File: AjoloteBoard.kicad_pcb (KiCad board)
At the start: 2 copper layers, 69 x 84.9 mm, 9 parts, among them SW1 On

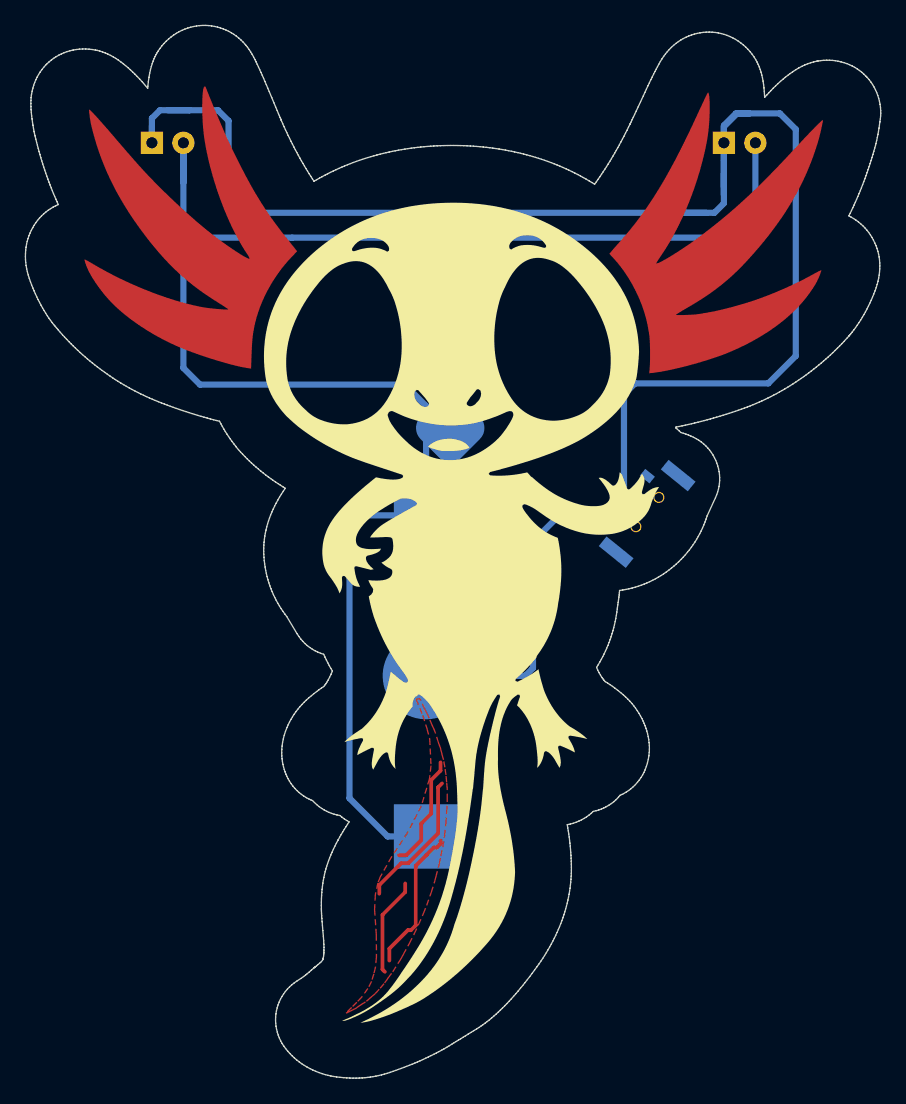
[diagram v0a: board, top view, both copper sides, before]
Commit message: Battery holder and switch changed
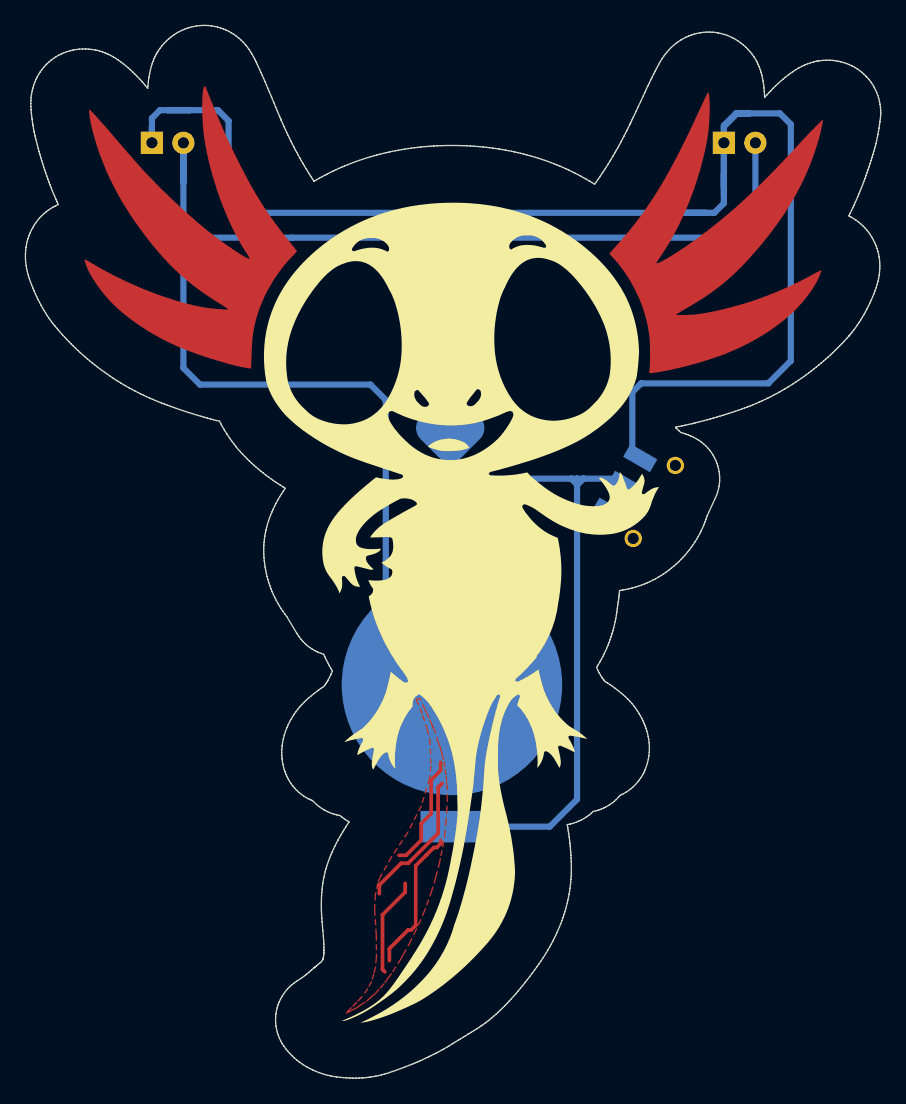
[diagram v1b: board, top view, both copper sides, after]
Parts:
- BT1: footprint footprints:79523141 -> Batteries:BAT-HLD-001
- SW1: footprint footprints:Micro_interruptor_SPDT -> footprints:JS102011SAQN
- moved SW1 4.40 mm to (173.7, 93.1), turned to -120 degrees
- moved BT1 2.21 mm to (158.9, 108.7)
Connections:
- D1 pad 1: Net-(D1-Pad1) -> Net-(D1-K)
- D2 pad 1: Net-(D1-Pad1) -> Net-(D1-K)
- SW1 pad 1: Net-(SW1-Pad1) -> Net-(D1-K)
- SW1 pad 3: Net-(D1-Pad1) -> unconnected-(SW1A-C-Pad3)
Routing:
- net Net-(D1-Pad1): track 125.4 -> 0.00 mm
- net Net-(D1-K): track 0.00 -> 121.0 mm
- net Net-(BT1--): track 26.2 -> 57.4 mm
- net Net-(BT1-+): track 141.4 -> 127.5 mm
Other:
- board text added: "v1.1"
- board text removed: "v1.0"

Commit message: Corrected battery routing
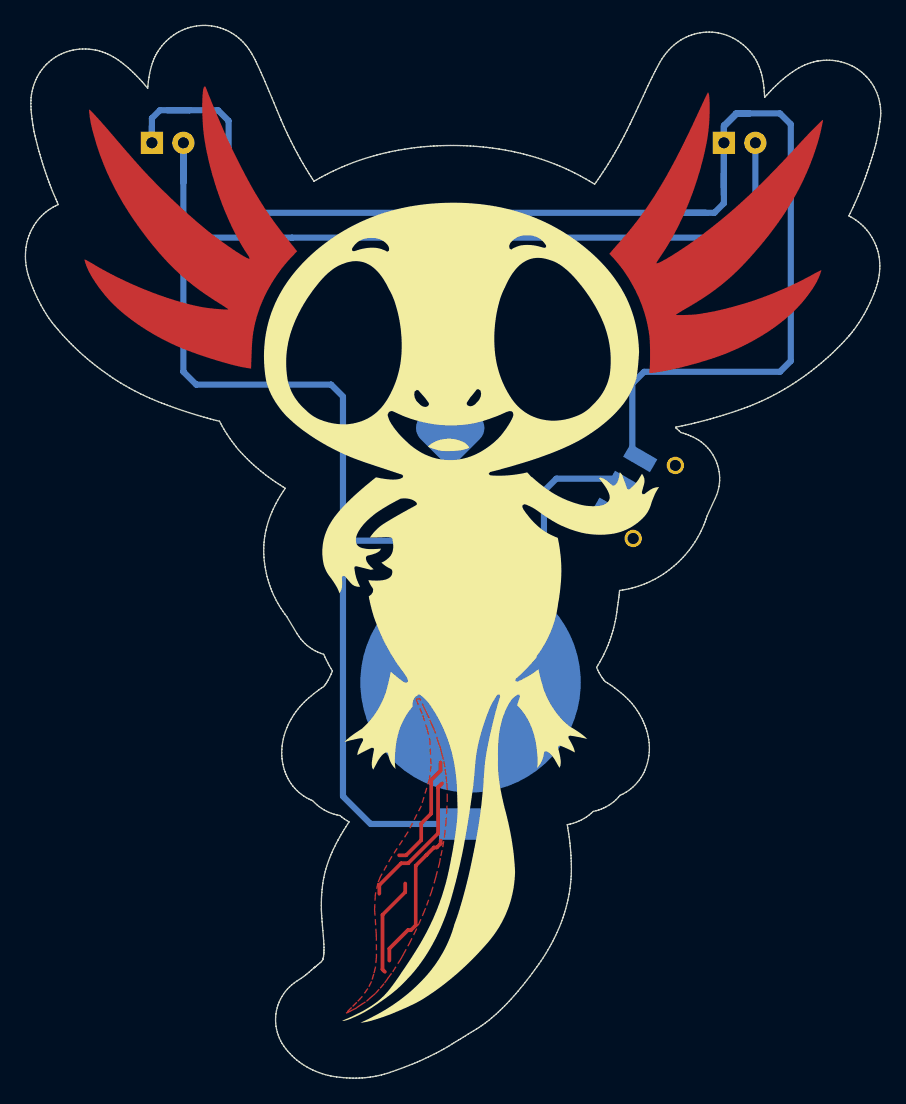
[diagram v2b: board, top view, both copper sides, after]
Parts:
- moved BT1 1.51 mm to (160.4, 108.5)
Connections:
- BT1 pad 1: Net-(BT1-+) -> Net-(BT1--)
- BT1 pad 2: Net-(BT1--) -> Net-(BT1-+)
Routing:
- net Net-(BT1--): track 57.4 -> 28.4 mm
- net Net-(BT1-+): track 127.5 -> 145.5 mm
